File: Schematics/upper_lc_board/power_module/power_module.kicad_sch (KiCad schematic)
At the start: 28 parts, among them U13 ID_LM66100DCKR, U14 ID_LM66100DCKR, U3 AMS1117-3.3

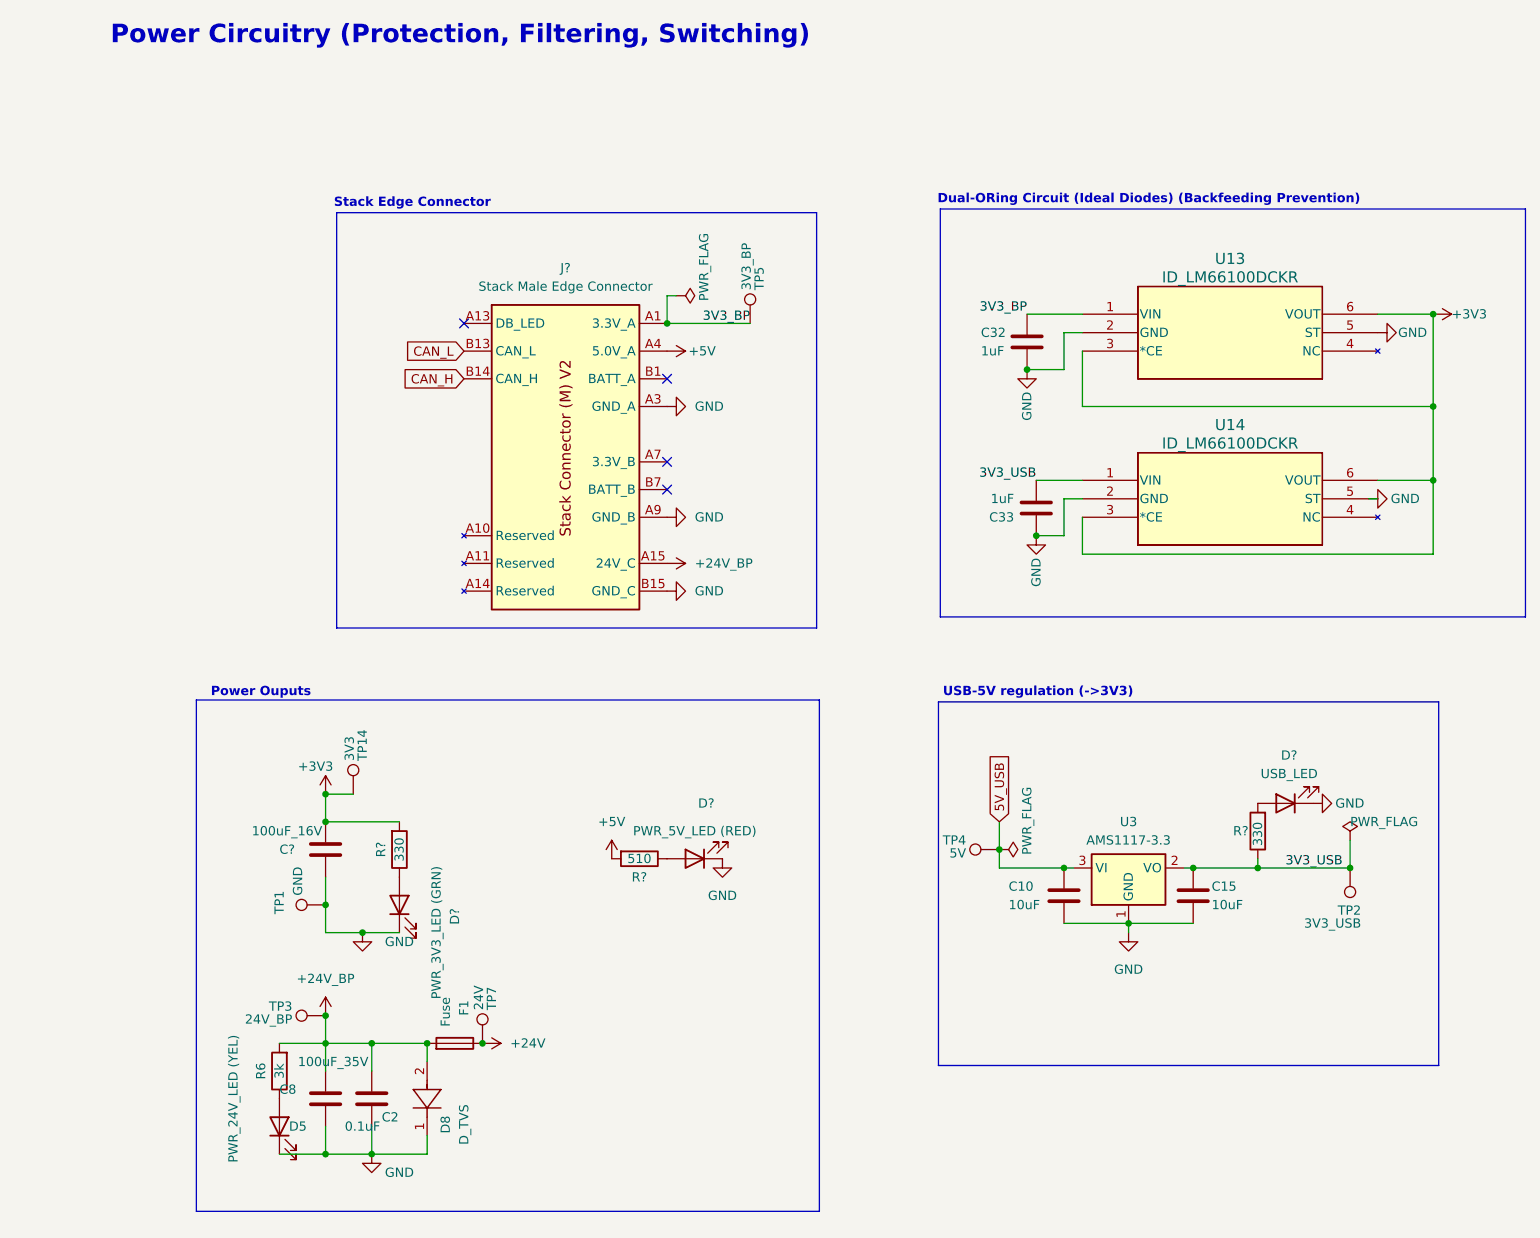
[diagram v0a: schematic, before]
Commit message: added most part number (LCSC, Digikey), verified current limiting resitors
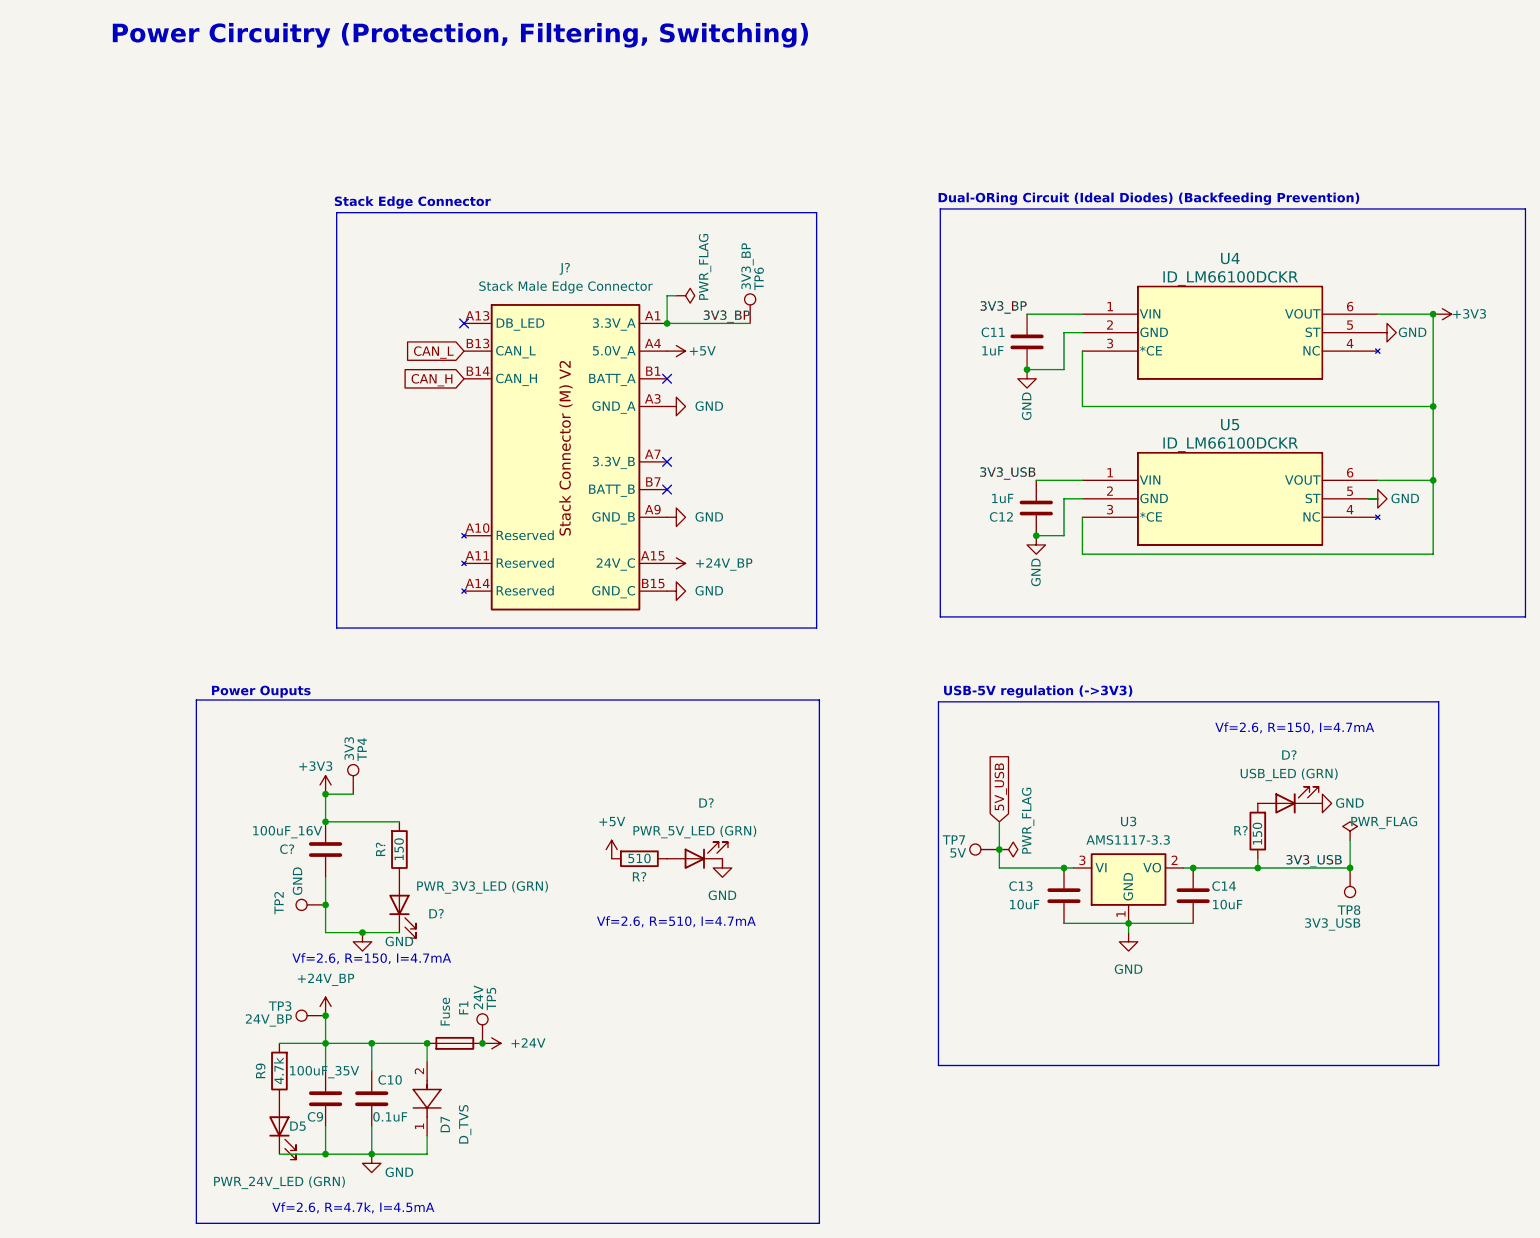
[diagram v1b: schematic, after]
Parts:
- removed R6: 3k, Resistor_SMD:R_0402_1005Metric, symbol Device:R
- added R9: 4.7k, Resistor_SMD:R_1206_3216Metric_Pad1.30x1.75mm_HandSolder, symbol Device:R
- C9: renamed from C8; Digikey (none) -> 732-8511-1-ND; LCSC 732-8511-1-ND -> (none)
- C?: Digikey (none) -> 732-8419-1-ND; LCSC 732-8419-1-ND -> (none)
- D5: value PWR_24V_LED (YEL) -> PWR_24V_LED (GRN); LCSC (none) -> C2297
- D7: renamed from D8; LCSC (none) -> C1973346
- D?: value USB_LED -> USB_LED (GRN); footprint LED_SMD:LED_0603_1608Metric -> LED_SMD:LED_0805_2012Metric; LCSC (none) -> C2297
- D?: value PWR_5V_LED (RED) -> PWR_5V_LED (GRN); LCSC (none) -> C2297
- D?: Digikey (none) -> 2297
- F1: LCSC (none) -> C3161527
- R? (x2): value 330 -> 150; LCSC C23138 -> C22808
- renumbered C2 to C10, C32 to C11, C33 to C12, C10 to C13, C15 to C14, TP1 to TP2, TP14 to TP4, TP7 to TP5, TP5 to TP6, TP4 to TP7, TP2 to TP8, U13 to U4, U14 to U5
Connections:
- net +24V_BP: now also R9.2
- net at D5.2 (A): now also R9.1
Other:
- note added: "Vf=2.6, R=150, I=4.7mA"
- note added: "Vf=2.6, R=4.7k, I=4.5mA"
- note added: "Vf=2.6, R=510, I=4.7mA"

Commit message: final pcb routing and part numbers
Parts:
- removed TP7: 5V, TestPoint:TestPoint_Pad_D1.0mm, symbol Connector:TestPoint
- added C20: 100uF_16V, Capacitor_SMD:CP_Elec_6.3x5.9, symbol Device:C
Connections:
- net +24V: now also R9.2
- net +24V_BP: no longer R9.2
- net +5V: now also C20.1
- net GND: now also C20.2
- net CAN_H renamed CAN_+
- net CAN_L renamed CAN_-
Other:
- moved on the sheet: D?, R?

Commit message: fix failed merge, fix part number issues
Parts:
- D?: Digikey 2297 -> (none); LCSC (none) -> 2297
- U3: LCSC (none) -> C6186; LSCS C6186 -> (none)
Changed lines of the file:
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@@
 			)
 		)
-		(property "LSCS" "C6186"
+		(property "LCSC" "C6186"
 			(at 153.67 133.35 0)
 			(effects
@@
 			)
 		)
-		(property "Digikey" "2297"
+		(property "LCSC" "2297"
 			(at 53.34 138.43 0)
 			(effects

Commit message: clean up silkscreen and routing
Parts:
- U4, U5: JLCPCB C2869734 -> (none); LCSC (none) -> C2869734
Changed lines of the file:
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@@
 			)
 		)
-		(property "JLCPCB" "C2869734"
+		(property "LCSC" "C2869734"
 			(at 167.64 82.55 0)
 			(effects
@@
 			)
 		)
-		(property "JLCPCB" "C2869734"
+		(property "LCSC" "C2869734"
 			(at 167.64 59.69 0)
 			(effects

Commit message: fixed incorrect footprints and part numbers
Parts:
- D?: LCSC 2297 -> C2297
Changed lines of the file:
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@@
 			)
 		)
-		(property "LCSC" "2297"
+		(property "LCSC" "C2297"
 			(at 53.34 138.43 0)
 			(effects

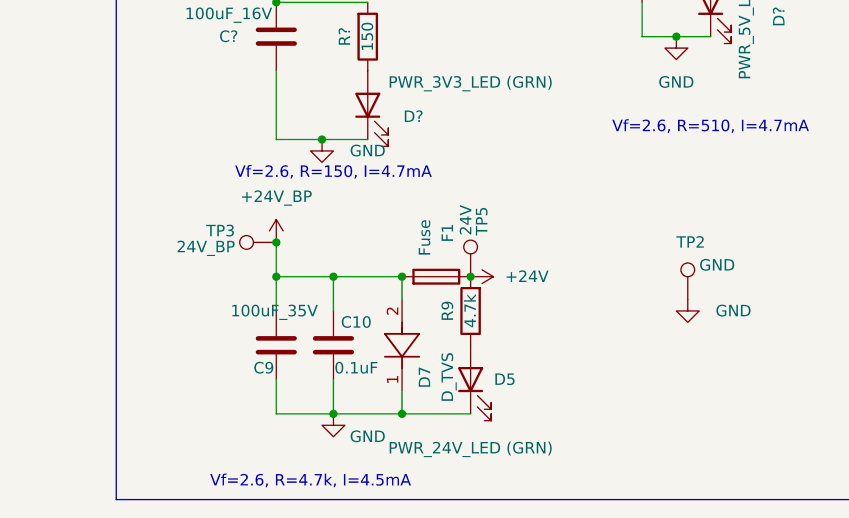
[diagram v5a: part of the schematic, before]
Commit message: updated opamp, 24v tvs diode, and excluded usbc antenna overlap error
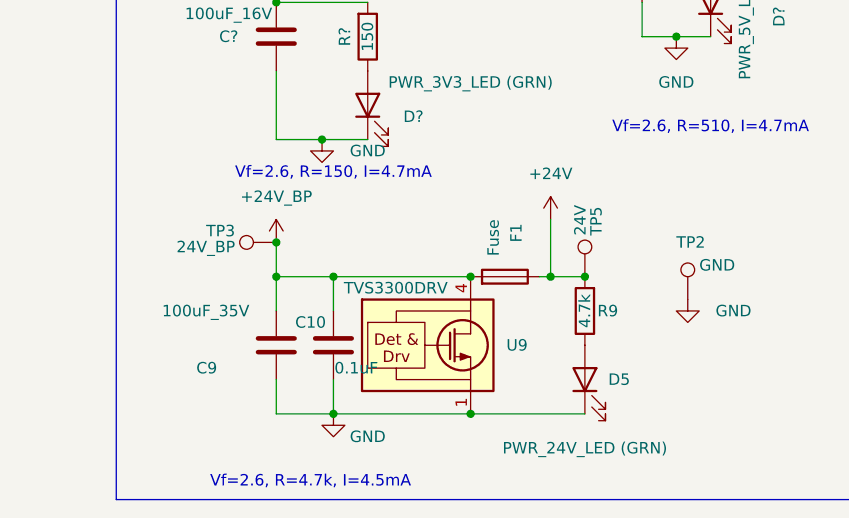
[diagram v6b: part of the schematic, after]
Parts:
- removed D7: D_TVS, SMA6L30A:SMASeries_LTF-L, symbol SMA6L30A:SMA6L30A
- added U9: TVS3300DRV, Package_SON:WSON-6-1EP_2x2mm_P0.65mm_EP1x1.6mm, symbol Power_Protection:TVS3300DRV
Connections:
- net +24V_BP: now also U9.4 (IN), U9.5 (IN), U9.6 (IN)
- net GND: now also U9.1 (GND), U9.2 (GND), U9.3 (GND), U9.7 (GND)
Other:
- moved on the sheet: D5, F1, R9, TP5

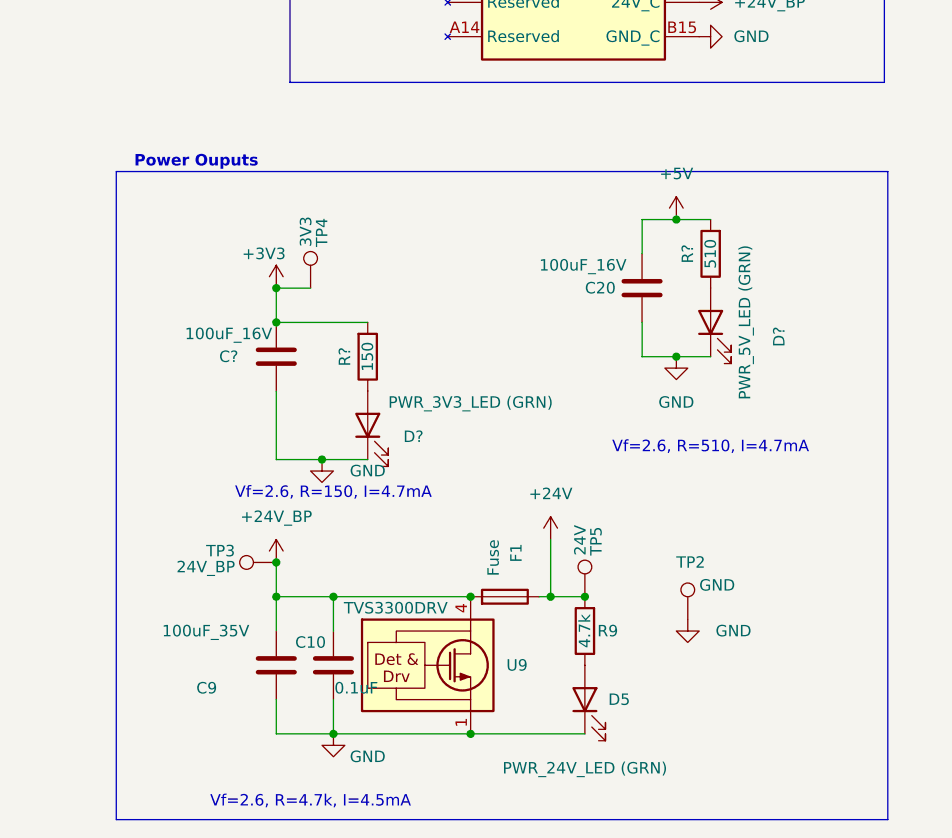
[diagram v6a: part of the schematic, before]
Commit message: fixed valve FB diode footprints, fixed major silkscreen warnings
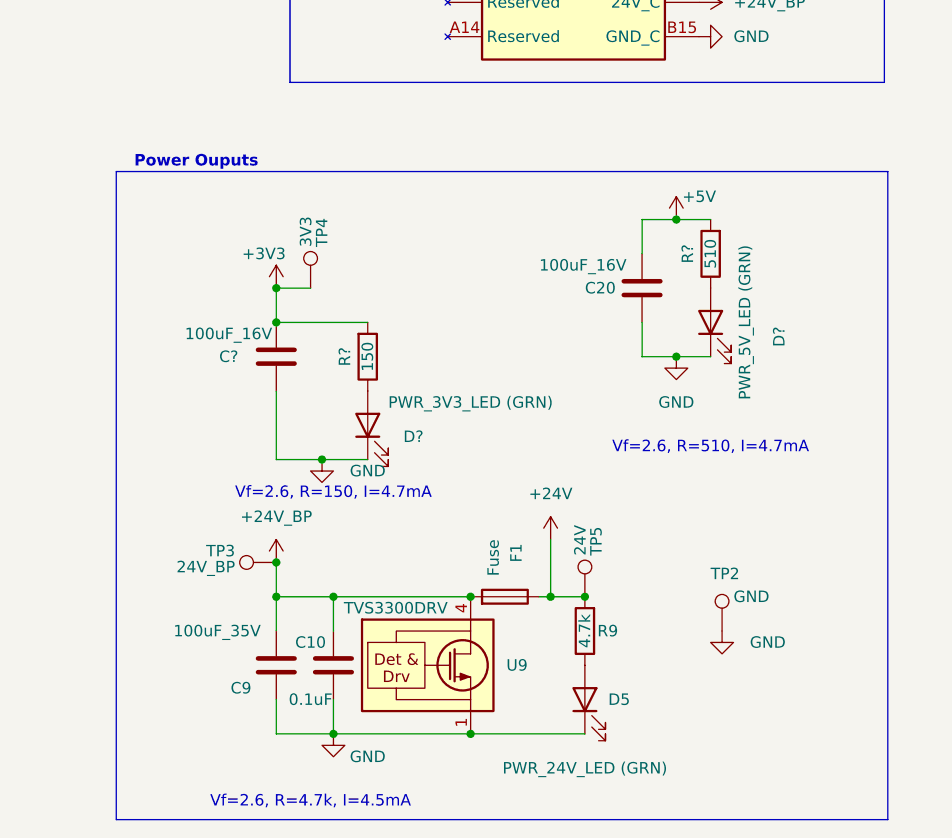
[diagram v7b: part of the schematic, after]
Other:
- moved on the sheet: TP2
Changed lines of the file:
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@@
 		(dnp no)
 		(property "Reference" "C9"
-			(at 34.29 167.64 0)
+			(at 38.1 167.64 0)
 			(effects
 				(font
@@
 		)
 		(property "Value" "100uF_35V"
-			(at 30.48 161.29 0)
+			(at 31.75 161.29 0)
 			(effects
 				(font
@@
 	(symbol
 		(lib_id "power:GND")
-		(at 88.9 160.02 0)
+		(at 92.71 161.29 0)
 		(unit 1)
 		(exclude_from_sim no)
@@
 		(dnp no)
 		(property "Reference" "#PWR87"
-			(at 88.9 166.37 0)
+			(at 92.71 167.64 0)
 			(effects
 				(font
@@
 		)
 		(property "Value" "GND"
-			(at 93.98 161.29 0)
+			(at 97.79 162.56 0)
 			(effects
 				(font
@@
 		)
 		(property "Footprint" ""
-			(at 88.9 160.02 0)
+			(at 92.71 161.29 0)
 			(effects
 				(font
@@
 		)
 		(property "Datasheet" ""
-			(at 88.9 160.02 0)
+			(at 92.71 161.29 0)
 			(effects
 				(font
@@
 		)
 		(property "Description" "Power symbol creates a global label with name \"GND\" , ground"
-			(at 88.9 160.02 0)
+			(at 92.71 161.29 0)
 			(effects
 				(font
@@
 		)
 		(property "Value" "0.1uF"
-			(at 52.07 167.64 0)
+			(at 46.99 168.91 0)
 			(effects
 				(font
@@
 		)
 		(property "Value" "+5V"
-			(at 87.63 110.49 0)
+			(at 90.17 113.03 0)
 			(effects
 				(font
@@
 	(symbol
 		(lib_id "Connector:TestPoint")
-		(at 88.9 160.02 0)
+		(at 92.71 161.29 0)
 		(unit 1)
 		(exclude_from_sim no)
@@
 		(dnp no)
 		(property "Reference" "TP2"
-			(at 87.63 153.67 0)
+			(at 91.44 154.94 0)
 			(effects
 				(font
@@
 		)
 		(property "Value" "GND"
-			(at 90.17 156.21 0)
+			(at 93.98 157.48 0)
 			(effects
 				(font
@@
 		)
 		(property "Footprint" "TestPoint:TestPoint_Pad_D1.0mm"
-			(at 93.98 160.02 0)
+			(at 97.79 161.29 0)
 			(effects
 				(font
@@
 		)
 		(property "Datasheet" "~"
-			(at 93.98 160.02 0)
+			(at 97.79 161.29 0)
 			(effects
 				(font
@@
 		)
 		(property "Description" "test point"
-			(at 88.9 160.02 0)
+			(at 92.71 161.29 0)
 			(effects
 				(font

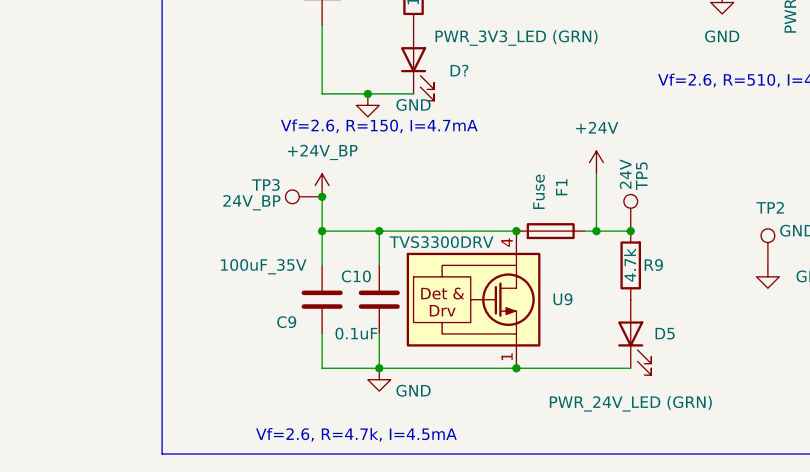
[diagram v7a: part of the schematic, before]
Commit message: updates after review using screw terminal for TC removed opamps for clamping diodes fixed solenoid FB diodes manual solder large SMDs on edges
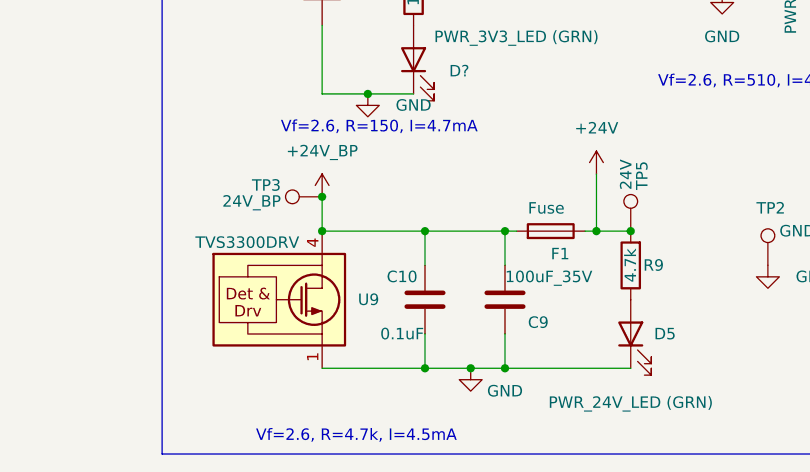
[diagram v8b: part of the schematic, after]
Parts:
- F1: Digikey (none) -> 5923-0679H2000-05CT-ND; LCSC C3161527 -> (none)
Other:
- moved on the sheet: C10, C9, U9
